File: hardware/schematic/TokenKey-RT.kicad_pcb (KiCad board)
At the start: 4 copper layers, 50 x 40 mm, 103 parts, among them J1 USB-C, J2 OLED 0.96in 128x64 I2C (SSD13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, J3 TC2030-NL, Q1 AO3401A, SW1 SW_BOOT, SW2 EC11E18244A5, SW3 BTN1, SW4 BTN2, U1 MIMXRT1062DVL6B, U2 AP2112K-3.3TRG1, U3 TLV62569DBVR, U4 W25Q64JVSSIQ, U5 APS6404L-3SQR-ZR, U6 USBLC6-2SC6, Y1 24MHz 12pF, Y2 32.768kHz 12.5pF

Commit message: PCB: J2 header and L2 from library after #47
- Merged origin/main (3ba9378, #47) into issue-43-pcb-sync. In
  decisions.md, took main's OLED rows.
- Schematic-to-board update (connector): J2 value is now "Header 1x04
  P2.54 H3.0 (OLED)" on Connector_PinHeader_2.54mm:PinHeader_1x04_P2.54mm_Vertical.
  Pin 1 stays at (16.34, 5.0), rot 90.
- Hand edit (pcbnew): J2 MPN PZ254-1-04-Z-C / LCSC C5156431 hidden fields.
- Hand edit (pcbnew): L2 updated from TokenKey:L_3.0x3.0mm_TDK_VLS3015CX
  (library now has attr smd), with the same position, rotation and nets.
  The connector cannot resolve the project TokenKey library.
- layout-notes: J2 header/3D-model note; the L2 mismatch is cleared.
- DRC: 0 errors, 6 warnings (J1 silk x2, H1-H4 lib). Parity is clean.

Fixes #43
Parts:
- J2: value OLED 0.96in 128x64 I2C (SSD1315) -> Header 1x04 P2.54 H3.0 (OLED)

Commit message: Routing phase 1: In1 GND plane, In2 3V3 plane + VDD_SOC island
Zones created with the connector's add_copper_pour. Hand edit (pcbnew): the
connector placed all three on F.Cu, so they were moved to In1.Cu/In2.Cu.
Also set VDD_SOC priority 1, min width 0.15, and names. Filled.

Part of #50 (WIP)
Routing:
- added copper zone on In2.Cu, net 3V3
- added copper zone on In1.Cu, net GND
- added copper zone on In2.Cu, net VDD_SOC
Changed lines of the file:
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@@
+		)
+	)
+	(zone
+		(net 29)
+		(net_name "GND")
+		(layer "In1.Cu")
+		(name "GND_PLANE_IN1")
+		(hatch edge 0.5)
+		(connect_pads
+			(clearance 0.1)
+		)
+		(min_thickness 0.15)
+		(filled_areas_thickness no)
+		(fill yes
+			(thermal_gap 0.5)
+			(thermal_bridge_width 0.5)
+		)
+		(polygon
+			(pts
+				(xy -0.05 -0.05) (xy 50.05 -0.05) (xy 50.05 40.05) (xy -0.05 40.05)
+			)
+		)
+	)
+	(zone
+		(net 6)
+		(net_name "VDD_SOC")
+		(layer "In2.Cu")
+		(name "VDD_SOC_ISLAND_IN2")
+		(hatch edge 0.5)
+		(priority 1)
+		(connect_pads
+			(clearance 0.1)
+		)
+		(min_thickness 0.15)
+		(filled_areas_thickness no)
+		(fill yes
+			(thermal_gap 0.5)
+			(thermal_bridge_width 0.5)
+		)
+		(polygon
+			(pts
+				(xy 6.8 18.5) (xy 11.2 18.5) (xy 11.2 19.4) (xy 15.5 19.4) (xy 15.5 18.75) (xy 18 18.75) (xy 18 20.85)
+				(xy 11.2 20.85) (xy 11.2 20) (xy 6.8 20)
+			)
+		)
+	)
+	(zone
+		(net 30)
+		(net_name "3V3")
+		(layer "In2.Cu")
+		(name "3V3_PLANE_IN2")
+		(hatch edge 0.5)
+		(connect_pads
+			(clearance 0.1)
+		)
+		(min_thickness 0.15)
+		(filled_areas_thickness no)
+		(fill yes
+			(thermal_gap 0.5)
+			(thermal_bridge_width 0.5)
+		)
+		(polygon
+			(pts
+				(xy -0.05 -0.05) (xy 50.05 -0.05) (xy 50.05 40.05) (xy -0.05 40.05)
+			)
 		)
 	)

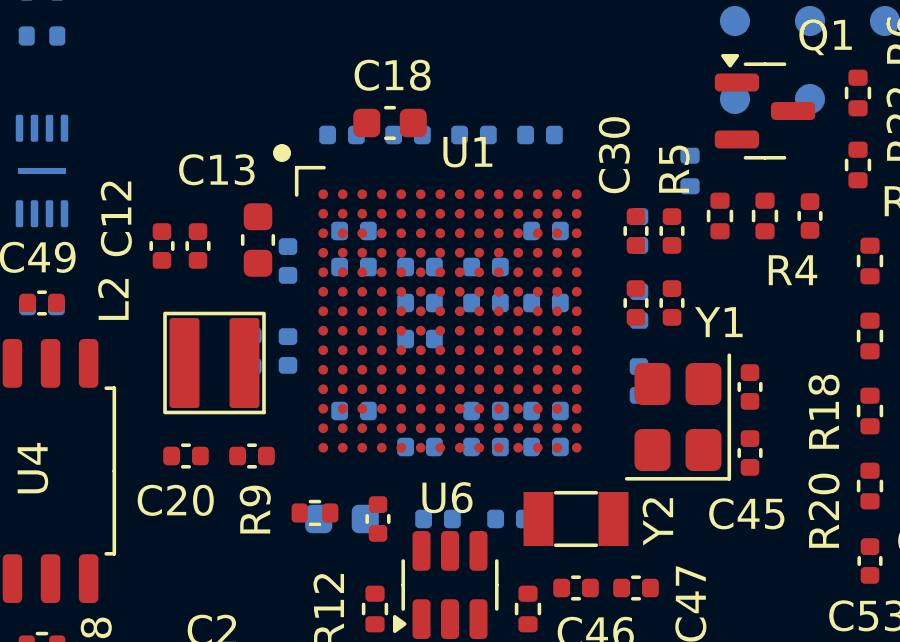
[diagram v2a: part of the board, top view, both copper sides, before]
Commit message: Routing phase 1 WIP: BGA power/GND ball fanout (0.30/0.15 vias + dogbones)
Hand edit (pcbnew): the connector's add_via has no size/drill parameters, so
BGA 0.30/0.15 vias can't be placed with it. 43 vias and 61 dogbones added.
USB escape sites (x 16.35/17.00/17.65, south of row L) are kept free.
VDD_SOC island outline was adjusted to the via pattern. Zones refilled.
Bottom decoupling caps still overlap the via field (re-placement pending),
so DRC is not clean at this WIP commit.

Part of #50 (WIP)
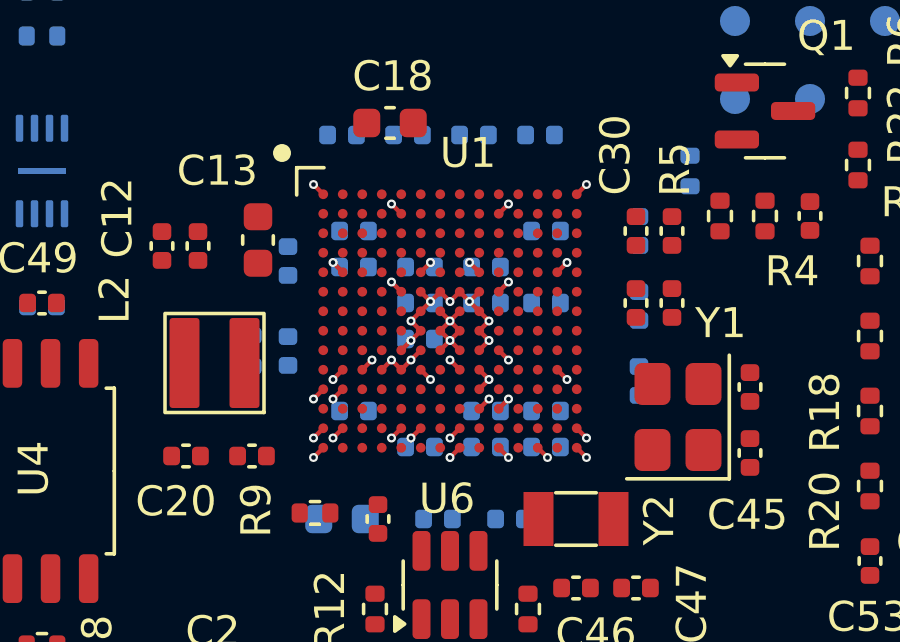
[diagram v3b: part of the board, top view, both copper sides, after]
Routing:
- net GND: track 0.00 -> 11.5 mm, vias 0 -> 18
- net VDD_SOC: track 0.00 -> 7.35 mm, vias 0 -> 7
- net 3V3: track 0.00 -> 6.43 mm, vias 0 -> 12
- net DCDC_PSWITCH: track 0.00 -> 0.46 mm, vias 0 -> 1
- net VDD_USB_CAP: track 0.00 -> 0.46 mm, vias 0 -> 1
- net VDD_SNVS_CAP: track 0.00 -> 0.46 mm, vias 0 -> 1
- net VDD_HIGH_CAP: track 0.00 -> 0.46 mm, vias 0 -> 1
- net NVCC_PLL: track 0.00 -> 0.46 mm, vias 0 -> 1
- net VBUS: track 0.00 -> 0.46 mm, vias 0 -> 1

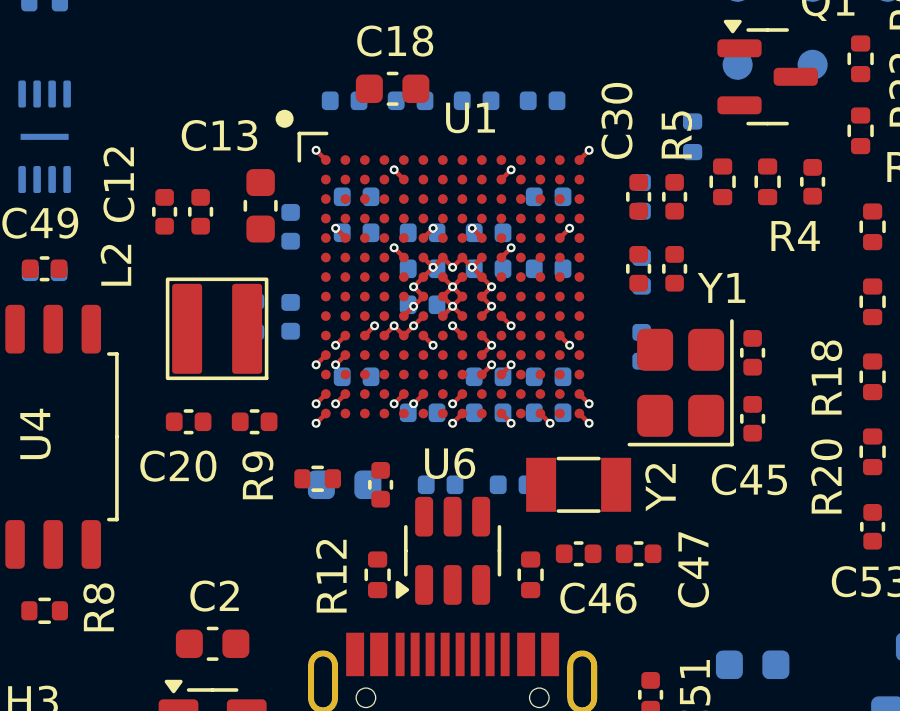
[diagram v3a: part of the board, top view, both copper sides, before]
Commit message: Routing phase 1 WIP: bottom decoupling caps re-placed onto the via grid and connected
Hand edit (pcbnew script, collision-checked): 18 bottom caps under or near
the BGA (C6-C10, C14-C16, C19, C21, C23-C25, C27, C40-C43) moved by up to
1.6 mm so their pads clear the 0.65 mm via grid (no via-in-pad). Each pad
gets a short B.Cu track to a same-net ball via, or to a new 0.30/0.15 via
(0.60/0.30 outside the U1 courtyard). Zones refilled.

Part of #50 (WIP)
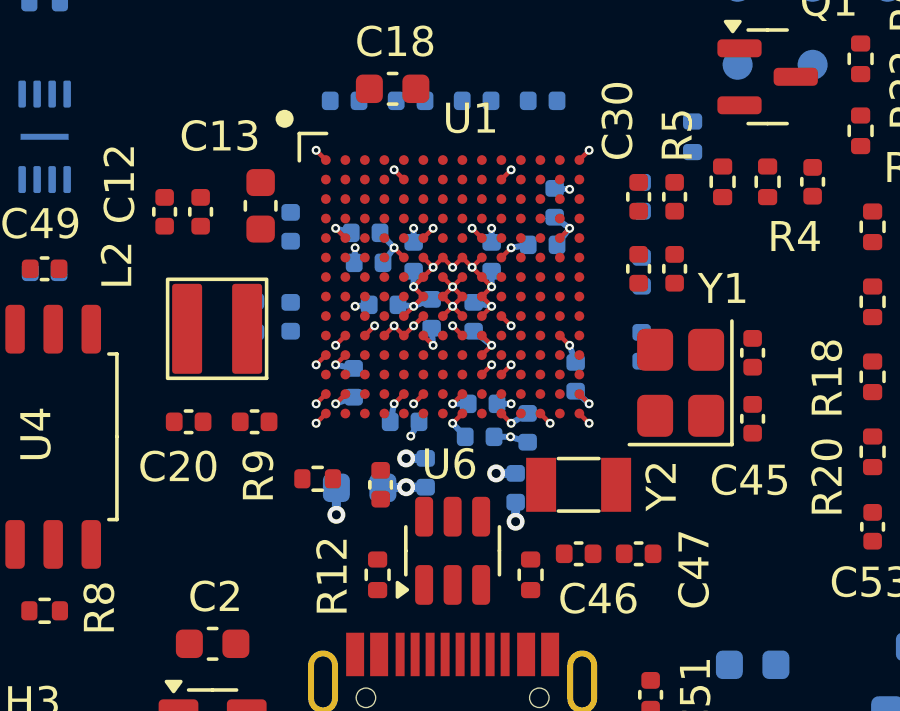
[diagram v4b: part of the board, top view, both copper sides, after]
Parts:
- moved C9 1.68 mm to (17.7, 21.0), turned to -90 degrees
- moved C8 1.53 mm to (16.3, 20.9), turned to -90 degrees
- moved C10 1.30 mm to (14.7, 20.6)
- moved C14 1.24 mm to (14.1, 18.2)
- moved C23 1.08 mm to (14.2, 19.2)
- moved C24 0.92 mm to (18.0, 23.9)
- moved C27 0.90 mm to (21.1, 23.0), turned to 90 degrees
- moved C43 0.86 mm to (19.5, 24.7), turned to -90 degrees
- moved C21 0.85 mm to (17.9, 25.0), turned to 0 degrees
- moved C6 0.85 mm to (15.7, 19.0), turned to 90 degrees
- moved C19 0.82 mm to (20.0, 18.6), turned to 0 degrees
- moved C7 0.81 mm to (18.3, 19.0), turned to 90 degrees
- moved C41 0.67 mm to (15.4, 24.5)
- moved C42 0.64 mm to (16.1, 26.2), turned to -90 degrees
- moved C40 0.51 mm to (13.9, 26.7), turned to 0 degrees
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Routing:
- net GND: track 11.5 -> 22.2 mm, vias 18 -> 25
- net 3V3: track 6.43 -> 10.0 mm, vias 12 -> 13
- net VDD_SOC: track 7.35 -> 10.2 mm
- net VDD_USB_CAP: track 0.46 -> 1.91 mm, vias 1 -> 3
- net NVCC_PLL: track 0.46 -> 1.75 mm, vias 1 -> 2
- net VDD_SNVS_CAP: track 0.46 -> 1.58 mm, vias 1 -> 3
- net VDD_HIGH_CAP: track 0.46 -> 1.08 mm

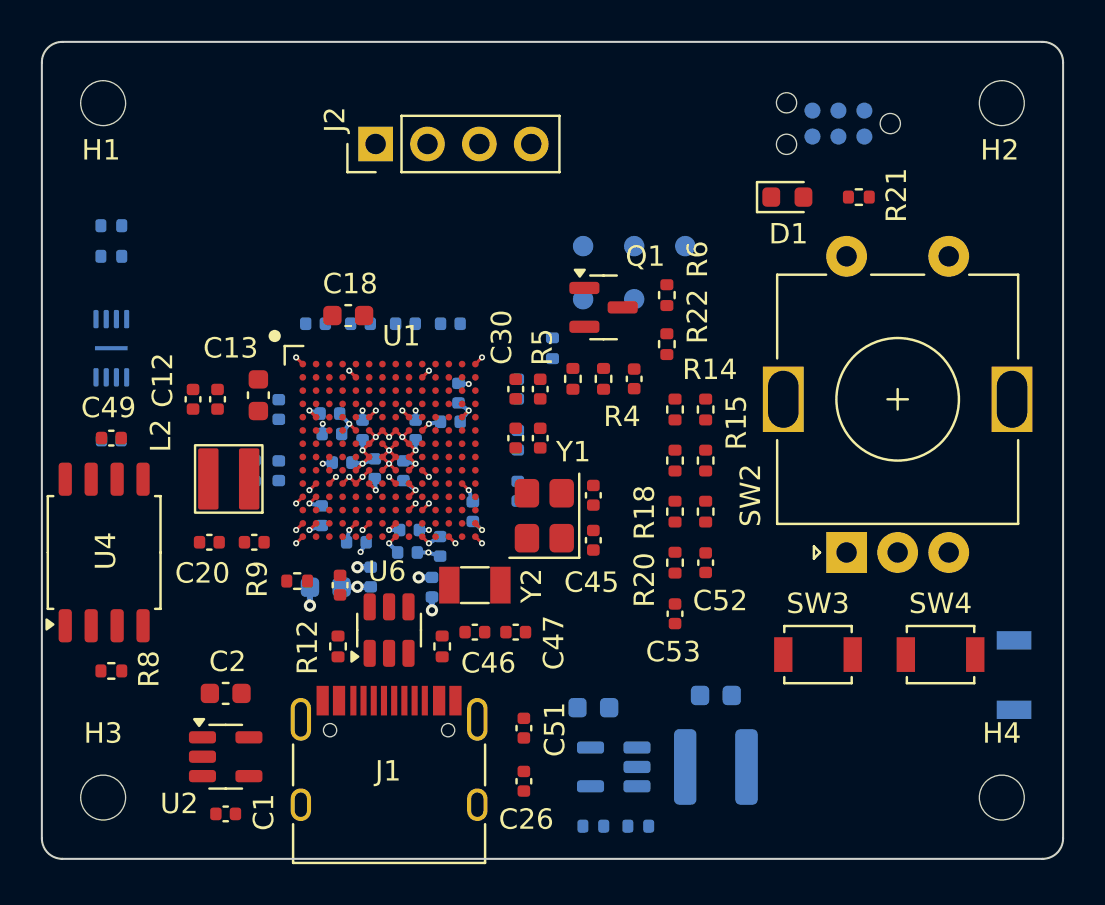
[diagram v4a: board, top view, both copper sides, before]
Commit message: Routing phase 1 WIP: plane vias for GND/3V3 pads, B.Cu decoupling rails
Hand edit (pcbnew script, collision-checked): 72 GND/3V3 pads outside the
ball field get a short track to an own plane via (0.60/0.30; 0.30/0.15 in
the U1 courtyard). GND via next to U6 USB_DP pad removed (0.5 mm USB
keep-away). B.Cu grid-routed rails: NVCC_PLL (C42-C43), VDD_SNVS_CAP
(M10-C24-C25), DCDC_PSWITCH (K3-C5-R3), VDD_USB_CAP (K8-C41-C40),
VDD_HIGH_CAP (P8-C21-C22). 0.15 mm inside the U1 courtyard, 0.30 outside.

Part of #57
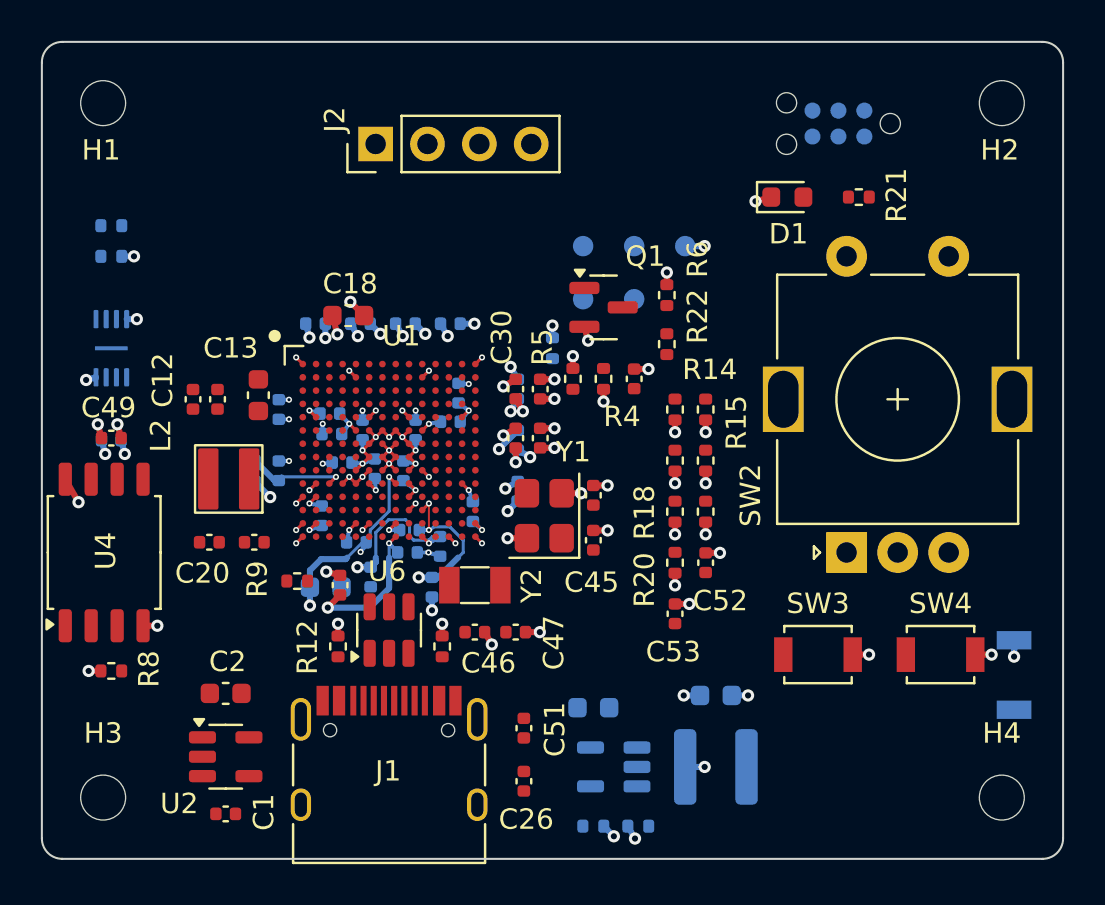
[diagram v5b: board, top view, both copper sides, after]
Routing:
- net GND: track 22.2 -> 49.2 mm, vias 25 -> 63
- net 3V3: track 10.0 -> 33.2 mm, vias 13 -> 46
- net VDD_USB_CAP: track 1.91 -> 10.3 mm
- net VDD_HIGH_CAP: track 1.08 -> 7.53 mm, vias 1 -> 2
- net VDD_SNVS_CAP: track 1.58 -> 8.00 mm
- net NVCC_PLL: track 1.75 -> 7.80 mm
- net DCDC_PSWITCH: track 0.46 -> 4.95 mm

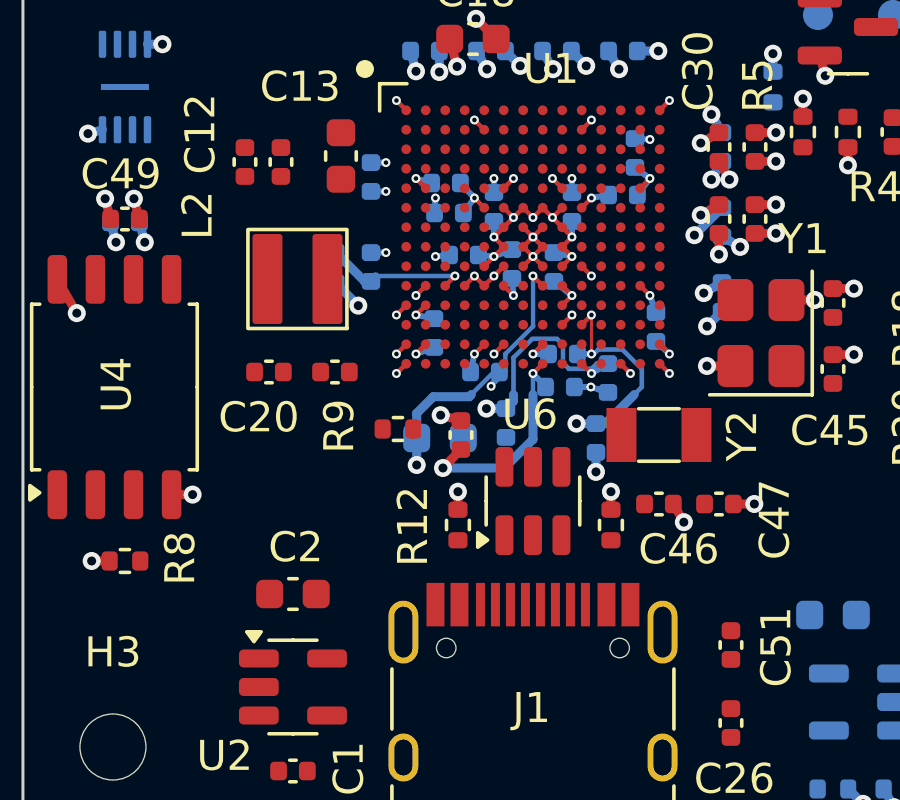
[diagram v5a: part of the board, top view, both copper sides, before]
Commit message: Routing phase 1: DCDC loop, VDD_SOC output, input caps; free the USB corridor
DCDC: L2.1 (DCDC_LP) to M1 on F.Cu, 0.50 mm outside the U1 courtyard,
0.25 mm neck between the L1/N1 dogbones, 0.10 mm M1-M2 link. L2.2 (VDD_SOC)
0.60 mm to a 0.50 mm bar on C12/C11/C13 pad 1, three 0.6/0.3 vias into the
In2 VDD_SOC island. C17/C20 (3V3 input) each get their own 3V3/GND via
north of the pads (C17.2 east, at the courtyard edge).

USB corridor (x 15.5-18.5 south of the BGA): removed three dangling vias
from c955b6a that sat in the DP/DN path (NVCC_PLL 15.45,25.72; VDD_SNVS_CAP
18.45,26.22; VDD_USB_CAP 13.125,27.6) with their tails. VDD_HIGH_CAP B.Cu
rail C21-C22 moved from x 17.0 to x 17.72 so the U6 VBUS pin can have a via.
J1 A1/B12 and A12/B1 GND pads tied to the shell pads on F.Cu. J1 VBUS pads
get 0.6/0.3 vias at y 30.9 and a 0.40 mm B.Cu link. U6 pin 2 (GND) via at
(17.0, 28.8) and pin 5 (VBUS) via at (17.0, 26.45), the only spots that keep
0.5 mm from the USB pads.

Hand edit (pcbnew script, collision-checked against the .kicad_dru values;
connector has no via size/tenting control or collision check). Zones refilled.

Part of #57
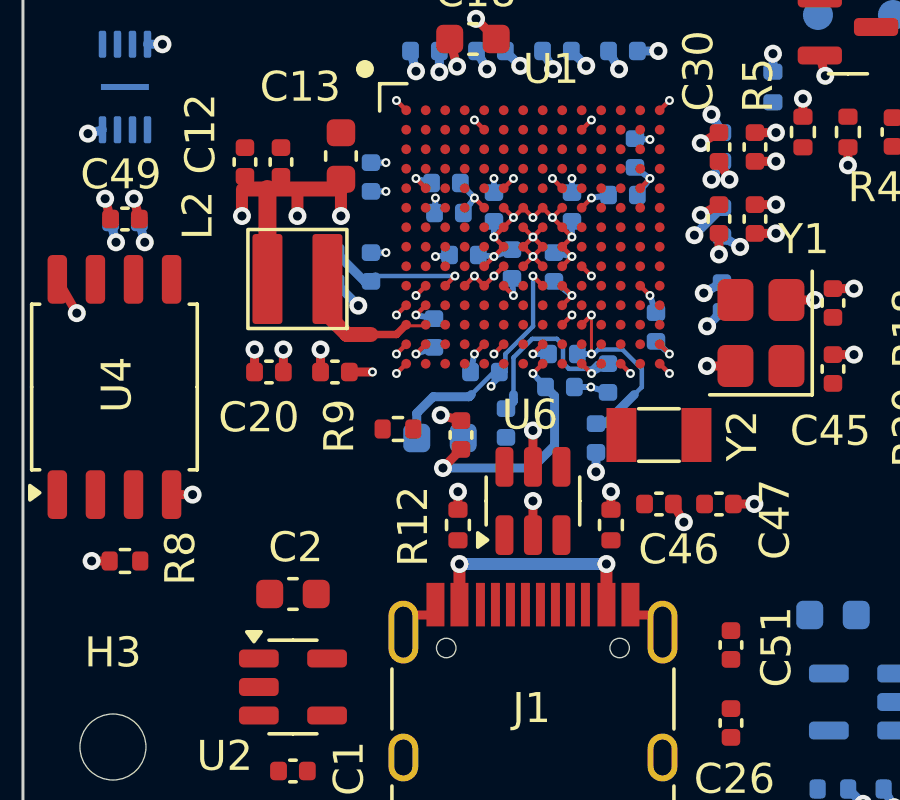
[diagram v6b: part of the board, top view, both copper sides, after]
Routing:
- net VBUS: track 0.46 -> 9.29 mm, vias 1 -> 4
- net VDD_SOC: track 10.2 -> 17.7 mm, vias 7 -> 10
- net GND: track 49.2 -> 54.0 mm, vias 63 -> 66
- net DCDC_LP: track 0.00 -> 3.68 mm
- net 3V3: track 33.2 -> 34.7 mm, vias 46 -> 48
- net VDD_USB_CAP: track 10.3 -> 9.42 mm, vias 3 -> 2
- net VDD_SNVS_CAP: track 8.00 -> 7.35 mm, vias 3 -> 2
- net NVCC_PLL: track 7.80 -> 7.15 mm, vias 2 -> 1
- net VDD_HIGH_CAP: track 7.53 -> 8.04 mm
